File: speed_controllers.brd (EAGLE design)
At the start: 147.3 x 147.3 mm, 31 parts, among them M1 TE-1-1123723-3, M2 TE-1-1123723-3, M3 TE-1-1123723-3, M4 TE-1-1123723-3, M5 TE-1-1123723-3, M6 TE-1-1123723-3, M7 TE-1-1123723-3, M8 TE-1-1123723-3

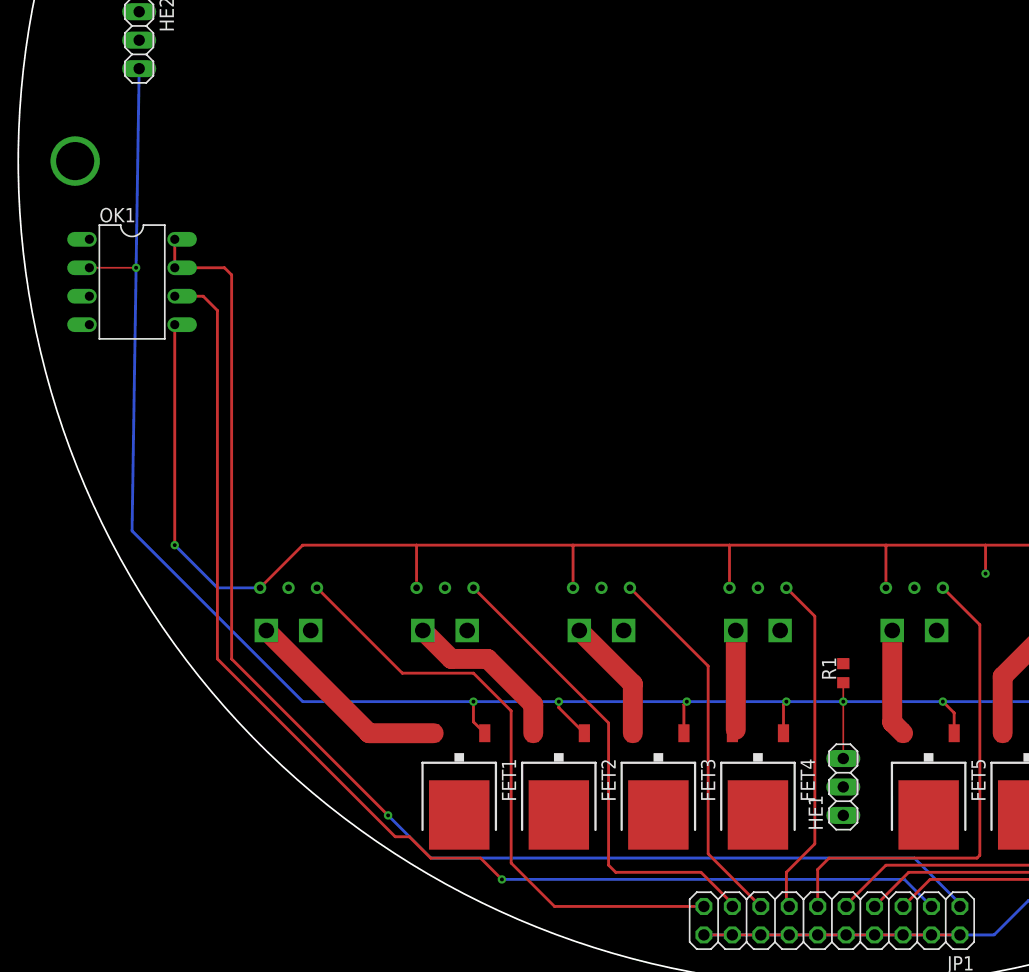
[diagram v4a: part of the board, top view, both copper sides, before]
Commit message: Changed optocoupler to SMD
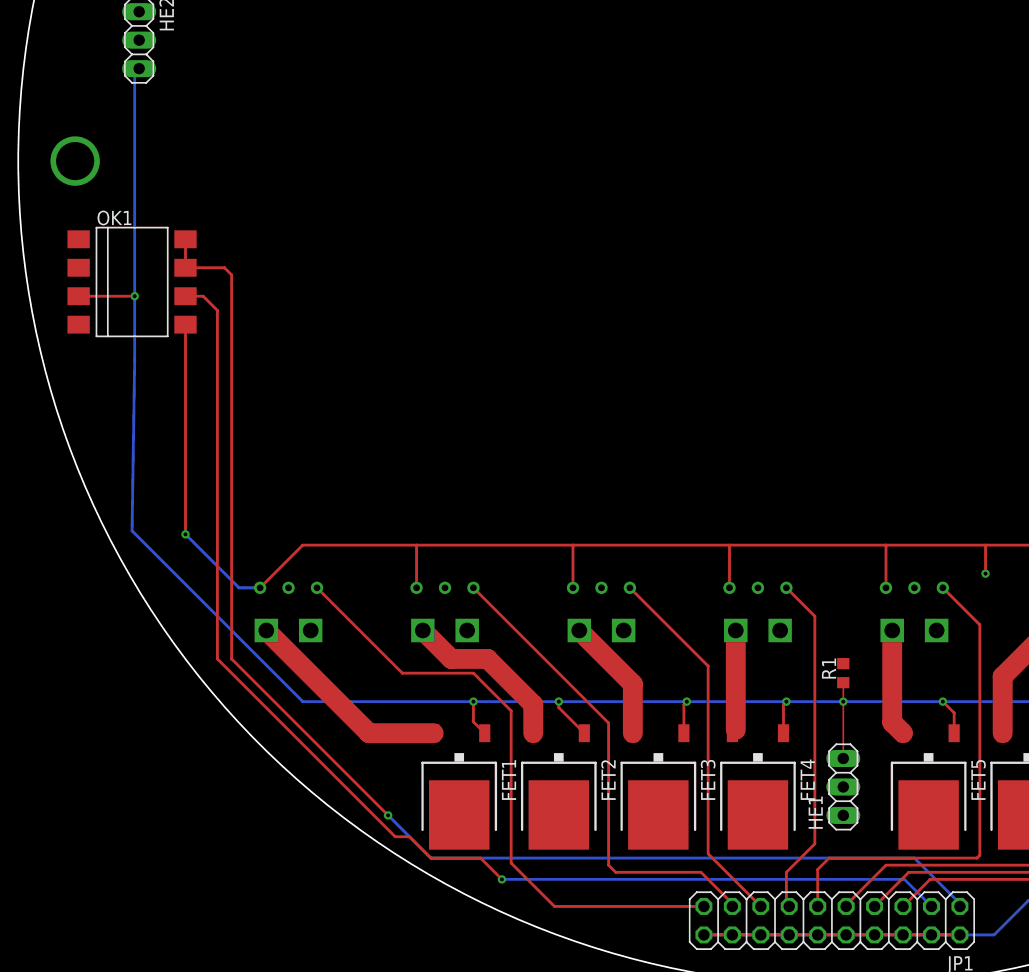
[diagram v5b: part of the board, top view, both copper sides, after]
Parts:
- OK1: value 6N137 -> 6N137SMD; device auv:DIL08 -> auv:DIL8-SMD
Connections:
- net FET_G: now also OK1.3; no longer OK1.2
- net GND: no longer OK1.3
- net VCC: now also OK1.2
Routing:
- net PWM_GND: track 258.0 -> 256.5 mm
- net FET_G: track 240.6 -> 241.6 mm
- net N$5: track 108.4 -> 107.4 mm
- net N$4: track 116.5 -> 115.5 mm
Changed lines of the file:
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@@
 <element name="HE3" library="auv" package="1X03" value="" x="60.96" y="-7.62" rot="R270"/>
 <element name="R1" library="auv" package="R0603" value="" x="0" y="-45.72" rot="R90"/>
-<element name="OK1" library="auv" package="DIL08" value="6N137" x="-63.5" y="-10.795" rot="R270">
-<attribute name="MF" value="" x="-63.5" y="-10.795" size="1.778" layer="27" rot="R270" display="off"/>
-<attribute name="MPN" value="6N137" x="-63.5" y="-10.795" size="1.778" layer="27" rot="R270" display="off"/>
-<attribute name="OC_FARNELL" value="1328376" x="-63.5" y="-10.795" size="1.778" layer="27" rot="R270" display="off"/>
-<attribute name="OC_NEWARK" value="52M1895" x="-63.5" y="-10.795" size="1.778" layer="27" rot="R270" display="off"/>
-</element>
 <element name="JP1" library="auv" package="2X10" value="" x="-1.016" y="-67.818" rot="R180"/>
+<element name="OK1" library="auv" package="DIL8-SMD" value="6N137SMD" x="-63.5" y="-10.795" rot="R270"/>
 </elements>
 <signals>
@@
 <contactref element="HE2" pad="2"/>
 <contactref element="HE3" pad="2"/>
-<contactref element="OK1" pad="3"/>
 </signal>
 <signal name="VCC">
@@
 <contactref element="HE3" pad="1"/>
 <contactref element="R1" pad="2"/>
+<contactref element="OK1" pad="2"/>
 </signal>
 <signal name="FET_G">
@@
 <wire x1="0" y1="-46.57" x2="0" y2="-48.26" width="0.1524" layer="1"/>
 <wire x1="0" y1="-48.26" x2="0" y2="-53.34" width="0.1524" layer="1"/>
-<wire x1="-62.865" y1="8.255" x2="-63.138475" y2="-9.52079375" width="0.254" layer="16"/>
-<wire x1="-63.138475" y1="-9.52079375" x2="-63.5" y2="-33.02" width="0.254" layer="16"/>
+<wire x1="-63.5" y1="-33.02" x2="-63.37303125" y2="-24.766953125" width="0.254" layer="16"/>
+<wire x1="-63.37303125" y1="-24.766953125" x2="-63.26559375" y2="-17.78360625" width="0.254" layer="16"/>
 <wire x1="-63.5" y1="-33.02" x2="-48.26" y2="-48.26" width="0.254" layer="16"/>
 <wire x1="-48.26" y1="-48.26" x2="-33.02" y2="-48.26" width="0.254" layer="16"/>
@@
 <wire x1="50.8" y1="-48.26" x2="60.96" y2="-38.1" width="0.254" layer="1"/>
 <wire x1="60.96" y1="-38.1" x2="60.96" y2="-10.16" width="0.254" layer="1"/>
-<contactref element="OK1" pad="2"/>
-<wire x1="-67.31" y1="-9.525" x2="-63.14268125" y2="-9.525" width="0.1524" layer="1"/>
-<wire x1="-63.14268125" y1="-9.525" x2="-63.138475" y2="-9.52079375" width="0.1524" layer="1"/>
-<via x="-63.138475" y="-9.52079375" extent="1-16" drill="0.35"/>
+<contactref element="OK1" pad="3"/>
+<wire x1="-63.26559375" y1="-17.78360625" x2="-63.26559375" y2="-12.065" width="0.254" layer="16"/>
+<wire x1="-63.26559375" y1="-12.065" x2="-63.26559375" y2="7.85440625" width="0.254" layer="16"/>
+<wire x1="-63.26559375" y1="7.85440625" x2="-62.865" y2="8.255" width="0.254" layer="16"/>
+<wire x1="-68.27" y1="-12.065" x2="-63.26559375" y2="-12.065" width="0.254" layer="1"/>
+<via x="-63.26559375" y="-12.065" extent="1-16" drill="0.35"/>
 </signal>
 <signal name="PWM_GND">
@@
 <contactref element="JP1" pad="18"/>
 <contactref element="JP1" pad="20"/>
-<contactref element="OK1" pad="5"/>
 <wire x1="10.414" y1="-69.088" x2="13.462" y2="-69.088" width="0.254" layer="16"/>
 <wire x1="13.462" y1="-69.088" x2="16.51" y2="-66.04" width="0.254" layer="16"/>
 <wire x1="10.414" y1="-69.088" x2="-12.446" y2="-69.088" width="0.254" layer="16"/>
-<wire x1="-59.69" y1="-14.605" x2="-59.69" y2="-34.29" width="0.254" layer="1"/>
-<via x="-59.69" y="-34.29" extent="1-16" drill="0.35"/>
-<wire x1="-59.69" y1="-34.29" x2="-55.88" y2="-38.1" width="0.254" layer="16"/>
-<wire x1="-55.88" y1="-38.1" x2="-52.07" y2="-38.1" width="0.254" layer="16"/>
 <wire x1="-12.446" y1="-69.088" x2="-9.906" y2="-69.088" width="0.254" layer="1"/>
 <wire x1="-9.906" y1="-69.088" x2="-7.366" y2="-69.088" width="0.254" layer="1"/>
@@
 <wire x1="5.334" y1="-69.088" x2="7.874" y2="-69.088" width="0.254" layer="1"/>
 <wire x1="7.874" y1="-69.088" x2="10.414" y2="-69.088" width="0.254" layer="1"/>
+<contactref element="OK1" pad="5"/>
+<wire x1="-58.73" y1="-14.605" x2="-58.73" y2="-33.33" width="0.254" layer="1"/>
+<via x="-58.73" y="-33.33" extent="1-16" drill="0.35"/>
+<wire x1="-58.73" y1="-33.33" x2="-53.96" y2="-38.1" width="0.254" layer="16"/>
+<wire x1="-53.96" y1="-38.1" x2="-52.07" y2="-38.1" width="0.254" layer="16"/>
 </signal>
 <signal name="VIN_7">
@@
 </signal>
 <signal name="N$4">
-<contactref element="OK1" pad="7"/>
-<contactref element="OK1" pad="8"/>
 <contactref element="JP1" pad="1"/>
-<wire x1="-59.69" y1="-6.985" x2="-59.69" y2="-9.525" width="0.254" layer="1"/>
-<wire x1="-59.69" y1="-9.525" x2="-55.245" y2="-9.525" width="0.254" layer="1"/>
-<wire x1="-55.245" y1="-9.525" x2="-54.61" y2="-10.16" width="0.254" layer="1"/>
+<wire x1="-54.61" y1="-10.16" x2="-55.245" y2="-9.525" width="0.254" layer="1"/>
 <wire x1="-54.61" y1="-10.16" x2="-54.61" y2="-44.45" width="0.254" layer="1"/>
 <via x="-40.64" y="-58.42" extent="1-16" drill="0.35"/>
-<wire x1="6.985" y1="-62.865" x2="10.414" y2="-66.294" width="0.254" layer="16"/>
+<wire x1="6.35" y1="-62.23" x2="10.414" y2="-66.294" width="0.254" layer="16"/>
 <wire x1="10.414" y1="-66.294" x2="10.414" y2="-66.548" width="0.254" layer="16"/>
 <wire x1="-54.61" y1="-44.45" x2="-40.64" y2="-58.42" width="0.254" layer="1"/>
-<wire x1="-40.64" y1="-58.42" x2="-38.735" y2="-60.325" width="0.254" layer="16"/>
-<wire x1="-38.735" y1="-60.325" x2="-36.83" y2="-62.23" width="0.254" layer="16"/>
-<wire x1="6.35" y1="-62.23" x2="6.985" y2="-62.865" width="0.254" layer="16"/>
+<wire x1="-40.64" y1="-58.42" x2="-36.83" y2="-62.23" width="0.254" layer="16"/>
 <wire x1="-36.83" y1="-62.23" x2="6.35" y2="-62.23" width="0.254" layer="16"/>
+<contactref element="OK1" pad="8"/>
+<contactref element="OK1" pad="7"/>
+<wire x1="-55.245" y1="-9.525" x2="-58.73" y2="-9.525" width="0.254" layer="1"/>
+<wire x1="-58.73" y1="-9.525" x2="-58.73" y2="-6.985" width="0.254" layer="1"/>
 </signal>
 <signal name="N$5">
-<contactref element="OK1" pad="6"/>
 <contactref element="JP1" pad="3"/>
 <wire x1="7.874" y1="-66.548" x2="5.461" y2="-64.135" width="0.254" layer="16"/>
@@
 <via x="-30.48" y="-64.135" extent="1-16" drill="0.35"/>
 <wire x1="-40.005" y1="-60.325" x2="-55.88" y2="-44.45" width="0.254" layer="1"/>
-<wire x1="-55.88" y1="-44.45" x2="-55.88" y2="-13.335" width="0.254" layer="1"/>
-<wire x1="-55.88" y1="-13.335" x2="-57.15" y2="-12.065" width="0.254" layer="1"/>
-<wire x1="-57.15" y1="-12.065" x2="-59.69" y2="-12.065" width="0.254" layer="1"/>
+<wire x1="-55.88" y1="-13.335" x2="-55.88" y2="-44.45" width="0.254" layer="1"/>
 <wire x1="-38.735" y1="-60.325" x2="-40.005" y2="-60.325" width="0.254" layer="1"/>
 <wire x1="-32.385" y1="-62.23" x2="-36.83" y2="-62.23" width="0.254" layer="1"/>
 <wire x1="-36.83" y1="-62.23" x2="-38.735" y2="-60.325" width="0.254" layer="1"/>
 <wire x1="-30.48" y1="-64.135" x2="-32.385" y2="-62.23" width="0.254" layer="1"/>
+<contactref element="OK1" pad="6"/>
+<wire x1="-58.73" y1="-12.065" x2="-57.15" y2="-12.065" width="0.254" layer="1"/>
+<wire x1="-57.15" y1="-12.065" x2="-55.88" y2="-13.335" width="0.254" layer="1"/>
 </signal>
 </signals>
